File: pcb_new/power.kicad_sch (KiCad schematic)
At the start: 37 parts, among them J2 632723300011, J3 1689310, U11 TPS2023DR, U12 LM1085ISX-3.3/NOPB, U13 INA226AIDGSR

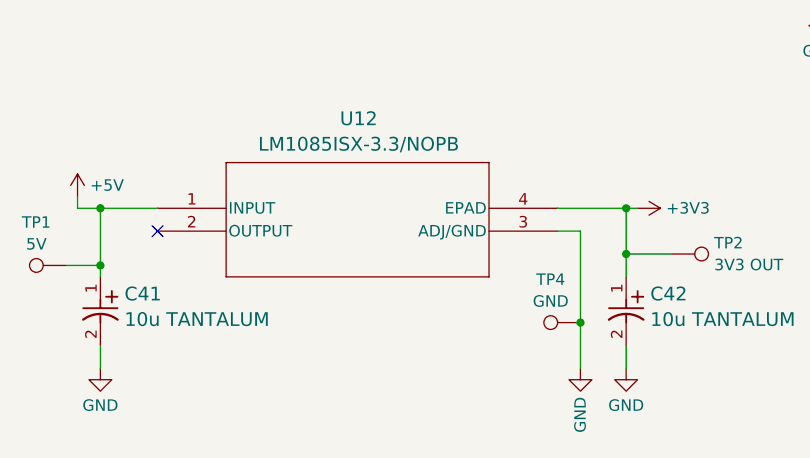
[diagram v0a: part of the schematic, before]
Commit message: fix LDO pins (ref #54)
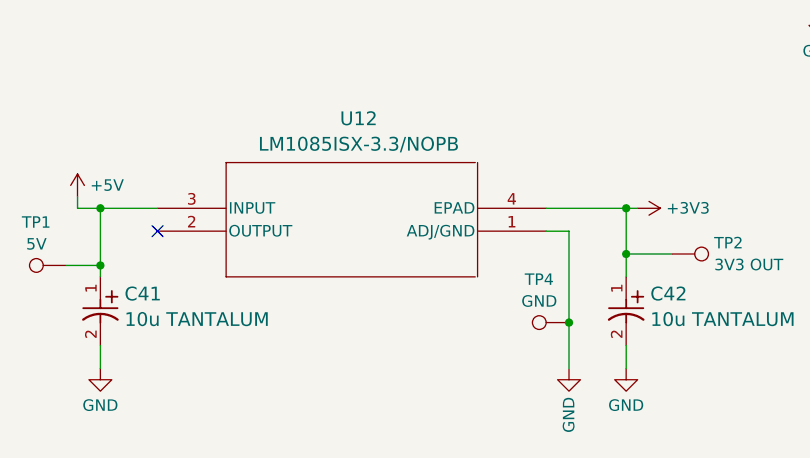
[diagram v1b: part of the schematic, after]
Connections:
- net +5V: now also U12.3 (INPUT); no longer U12.1 (INPUT)
- net GND: now also U12.1 (ADJ/GND); no longer U12.3 (ADJ/GND)
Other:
- moved on the sheet: TP4, U12
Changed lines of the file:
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@@
 	)
 	(junction
-		(at 102.87 171.45)
+		(at 101.6 171.45)
 		(diameter 0)
 		(color 0 0 0 0)
@@
 	(wire
 		(pts
+			(xy 99.06 158.75) (xy 107.95 158.75)
+		)
+		(stroke
+			(width 0)
+			(type default)
+		)
+	)
+	(wire
+		(pts
 			(xy 152.4 34.29) (xy 152.4 38.1)
 		)
@@
 	(wire
 		(pts
-			(xy 102.87 161.29) (xy 100.33 161.29)
+			(xy 101.6 161.29) (xy 99.06 161.29)
 		)
 		(stroke
@@
 	(wire
 		(pts
-			(xy 102.87 161.29) (xy 102.87 171.45)
+			(xy 101.6 161.29) (xy 101.6 171.45)
 		)
 		(stroke
@@
 	(wire
 		(pts
-			(xy 100.33 158.75) (xy 107.95 158.75)
-		)
-		(stroke
-			(width 0)
-			(type default)
-		)
-	)
-	(wire
-		(pts
 			(xy 262.89 76.2) (xy 262.89 81.28)
 		)
@@
 	(wire
 		(pts
-			(xy 102.87 171.45) (xy 102.87 176.53)
+			(xy 101.6 171.45) (xy 101.6 176.53)
 		)
 		(stroke
@@
 	(symbol
 		(lib_id "Connector:TestPoint")
-		(at 102.87 171.45 90)
+		(at 101.6 171.45 90)
 		(unit 1)
 		(exclude_from_sim no)
@@
 		(fields_autoplaced yes)
 		(property "Reference" "TP4"
-			(at 99.568 166.6705 90)
+			(at 98.298 166.6705 90)
 			(effects
 				(font
@@
 		)
 		(property "Value" "GND"
-			(at 99.568 169.0948 90)
+			(at 98.298 169.0948 90)
 			(effects
 				(font
@@
 		)
 		(property "Footprint" "TestPoint:TestPoint_Pad_1.0x1.0mm"
-			(at 102.87 166.37 0)
+			(at 101.6 166.37 0)
 			(effects
 				(font
@@
 		)
 		(property "Datasheet" "~"
-			(at 102.87 166.37 0)
+			(at 101.6 166.37 0)
 			(effects
 				(font
@@
 		)
 		(property "Description" "test point"
-			(at 102.87 171.45 0)
+			(at 101.6 171.45 0)
 			(effects
 				(font
@@
 	(symbol
 		(lib_id "power:GND")
-		(at 102.87 176.53 0)
+		(at 101.6 176.53 0)
 		(unit 1)
 		(exclude_from_sim no)
@@
 		(fields_autoplaced yes)
 		(property "Reference" "#PWR054"
-			(at 102.87 182.88 0)
+			(at 101.6 182.88 0)
 			(effects
 				(font
@@
 		)
 		(property "Value" "GND"
-			(at 102.87 179.7049 90)
+			(at 101.6 179.7049 90)
 			(effects
 				(font
@@
 		)
 		(property "Footprint" ""
-			(at 102.87 176.53 0)
+			(at 101.6 176.53 0)
 			(effects
 				(font
@@
 		)
 		(property "Datasheet" ""
-			(at 102.87 176.53 0)
+			(at 101.6 176.53 0)
 			(effects
 				(font
@@
 		)
 		(property "Description" "Power symbol creates a global label with name \"GND\" , ground"
-			(at 102.87 176.53 0)
+			(at 101.6 176.53 0)
 			(effects
 				(font

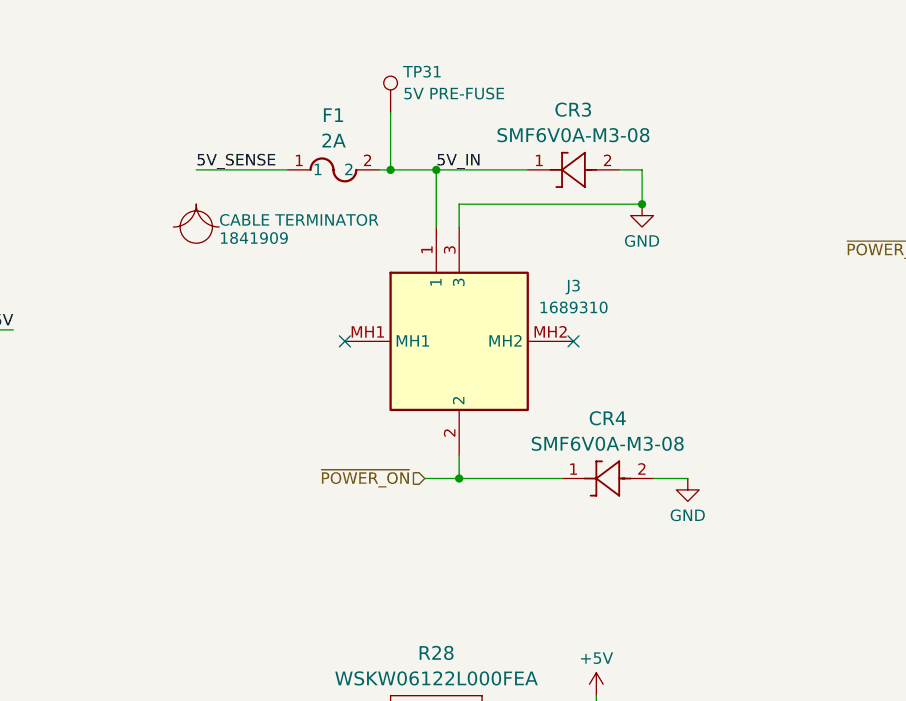
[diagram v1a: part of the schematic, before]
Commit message: switch to screw power terminal (ref #84)
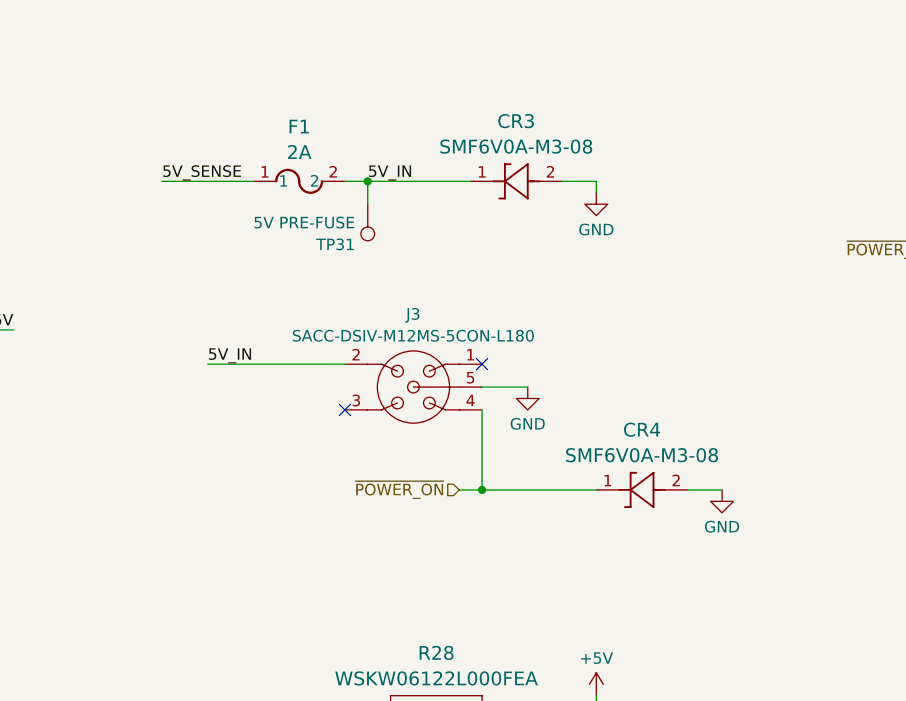
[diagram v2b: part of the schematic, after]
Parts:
- removed B2: 1841909, symbol Oro:BOM Part
- removed J3: 1689310, OroLink:1689310, symbol OroLink:1689310
- added J3: SACC-DSIV-M12MS-5CON-L180, OroLink:SACC-DSIV-M12MS-5CON-L180, symbol OroLink:SACC-DSIV-M12MS-5CON-L180
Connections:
- net 5V_IN: now also J3.2
- net GND: now also J3.5
- net ~{POWER_ON}: now also J3.4
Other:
- moved on the sheet: CR3, CR4, F1, TP31

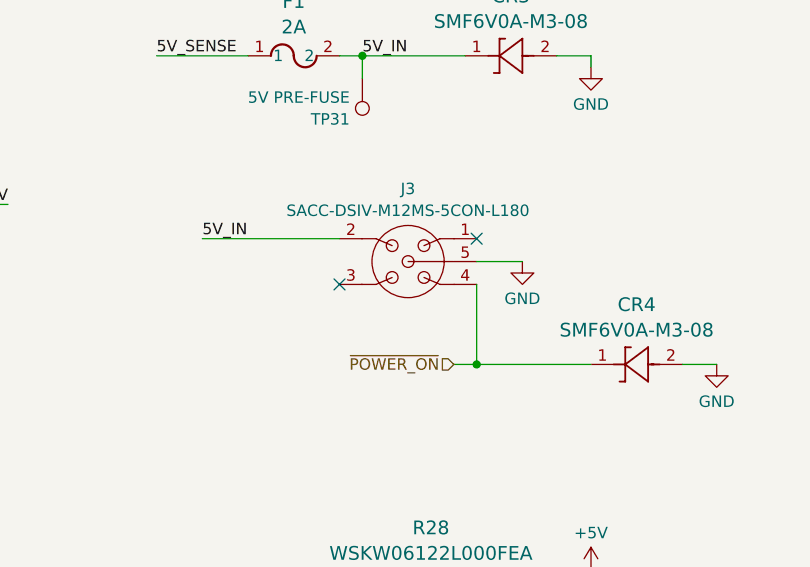
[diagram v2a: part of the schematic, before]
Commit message: pull pins 1 and 3 down to ground too (ref #84)
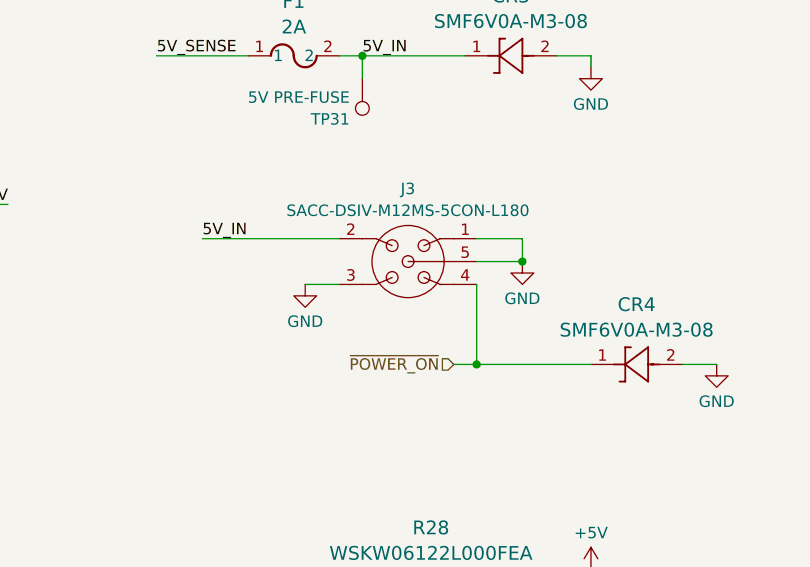
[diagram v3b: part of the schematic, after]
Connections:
- net GND: now also J3.1, J3.3
- no-connect marks 25 -> 23
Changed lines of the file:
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@@
 	)
 	(junction
+		(at 139.7 58.42)
+		(diameter 0)
+		(color 0 0 0 0)
+	)
+	(junction
 		(at 246.38 54.61)
 		(diameter 0)
@@
 	)
 	(no_connect
-		(at 134.62 55.88)
-	)
-	(no_connect
 		(at 240.03 83.82)
 	)
@@
 	)
 	(no_connect
-		(at 119.38 60.96)
-	)
-	(no_connect
 		(at 207.01 86.36)
 	)
 	(wire
 		(pts
+			(xy 119.38 60.96) (xy 115.57 60.96)
+		)
+		(stroke
+			(width 0)
+			(type default)
+		)
+	)
+	(wire
+		(pts
 			(xy 243.84 86.36) (xy 243.84 88.9)
 		)
@@
 	(wire
 		(pts
+			(xy 139.7 55.88) (xy 139.7 58.42)
+		)
+		(stroke
+			(width 0)
+			(type default)
+		)
+	)
+	(wire
+		(pts
 			(xy 189.23 90.17) (xy 189.23 91.44)
 		)
@@
 		)
 	)
+	(wire
+		(pts
+			(xy 134.62 55.88) (xy 139.7 55.88)
+		)
+		(stroke
+			(width 0)
+			(type default)
+		)
+	)
 	(polyline
 		(pts
@@
 					(unit 1)
 				)
+			)
+		)
+	)
+	(symbol
+		(lib_id "power:GND")
+		(at 115.57 60.96 0)
+		(unit 1)
+		(exclude_from_sim no)
+		(in_bom yes)
+		(on_board yes)
+		(dnp no)
+		(fields_autoplaced yes)
+		(property "Reference" "#PWR0197"
+			(at 115.57 67.31 0)
+			(effects
+				(font
+					(size 1.27 1.27)
+				)
+				(hide yes)
+			)
+		)
+		(property "Value" "GND"
+			(at 115.57 65.0931 0)
+			(effects
+				(font
+					(size 1.27 1.27)
+				)
+			)
+		)
+		(property "Footprint" ""
+			(at 115.57 60.96 0)
+			(effects
+				(font
+					(size 1.27 1.27)
+				)
+				(hide yes)
+			)
+		)
+		(property "Datasheet" ""
+			(at 115.57 60.96 0)
+			(effects
+				(font
+					(size 1.27 1.27)
+				)
+				(hide yes)
+			)
+		)
+		(property "Description" "Power symbol creates a global label with name \"GND\" , ground"
+			(at 115.57 60.96 0)
+			(effects
+				(font
+					(size 1.27 1.27)
+				)
+				(hide yes)
+			)
+		)
+		(pin "1"
+		)
+		(instances
+			(project "link"
+				(path "/b8dafc19-6de0-4c8f-9903-23372e5103df/efe900f0-e311-40d9-a69c-d0ffa18ab615"
+					(reference "#PWR0197")
+					(unit 1)
+				)

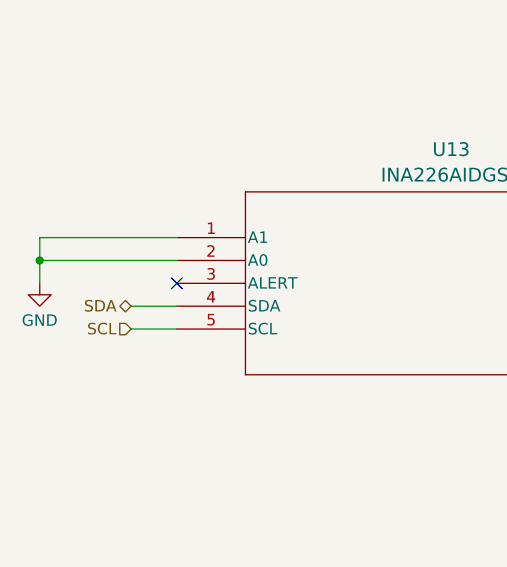
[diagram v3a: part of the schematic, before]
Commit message: add power monitor alert interrupt line (ref #82)
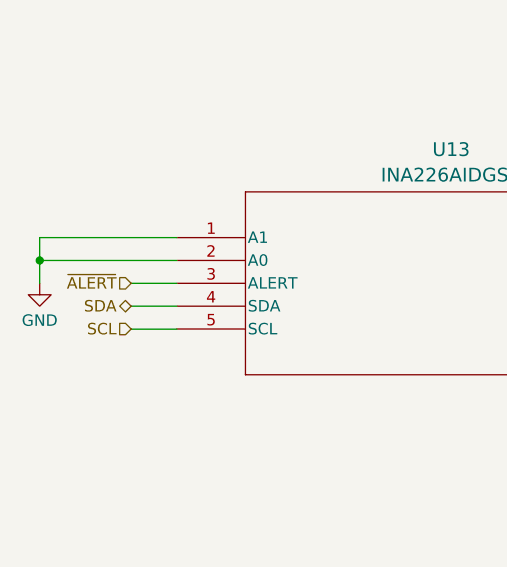
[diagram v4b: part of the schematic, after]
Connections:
- net ~{ALERT}: now reaches U13.3 (ALERT)
- no-connect marks 23 -> 22
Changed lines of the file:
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@@
-	)
-	(no_connect
-		(at 43.18 114.3)
 	)
 	(no_connect
@@
 		(pts
 			(xy 104.14 111.76) (xy 115.57 111.76)
+		)
+		(stroke
+			(width 0)
+			(type default)
+		)
+	)
+	(wire
+		(pts
+			(xy 38.1 114.3) (xy 43.18 114.3)
 		)
 		(stroke
@@
 		)
 	)
+	(hierarchical_label "~{ALERT}"
+		(shape input)
+		(at 38.1 114.3 180)
+		(fields_autoplaced yes)
+		(effects
+			(font
+				(size 1.27 1.27)
+			)
+			(justify right)
+		)
+	)
